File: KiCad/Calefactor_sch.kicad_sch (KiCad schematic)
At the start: 3 parts, among them U1 SHTC3

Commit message: calefactor-Usart
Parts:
- added Q13: AO3400A, Package_TO_SOT_SMD:SOT-23, symbol Transistor_FET:AO3400A
- added R7: Heater, symbol Device:Heater
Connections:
- net GND: now also R7.2
- new net: Q13.2 (S), R7.1
- new net 5V: Q13.3 (D)

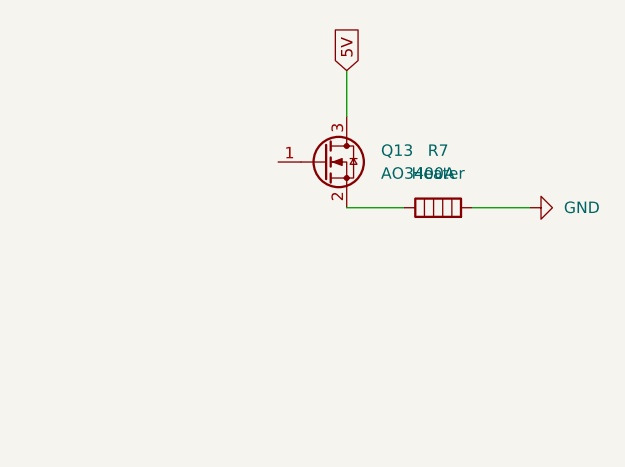
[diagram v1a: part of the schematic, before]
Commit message: añadido conexiones del PIC y cambiado lógica de los drivers para reducir pines
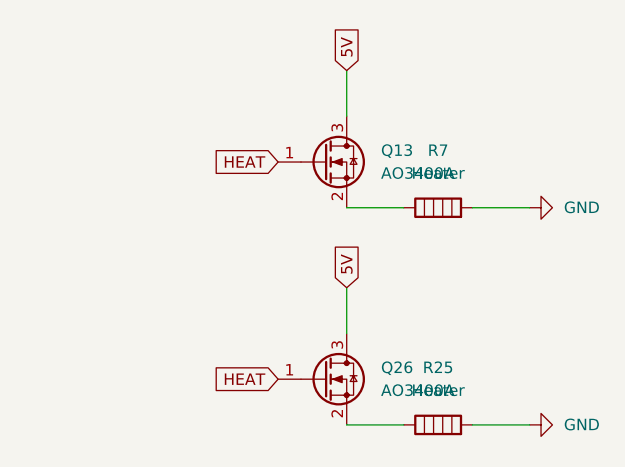
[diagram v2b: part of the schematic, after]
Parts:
- added Q26: AO3400A, Package_TO_SOT_SMD:SOT-23, symbol Transistor_FET:AO3400A
- added R25: Heater, symbol Device:Heater
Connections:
- net 5V: now also Q26.3 (D)
- net GND: now also R25.2
- net HEAT: now reaches Q13.1 (G)
- net HEAT: now also Q26.1 (G)
- new net: Q26.2 (S), R25.1

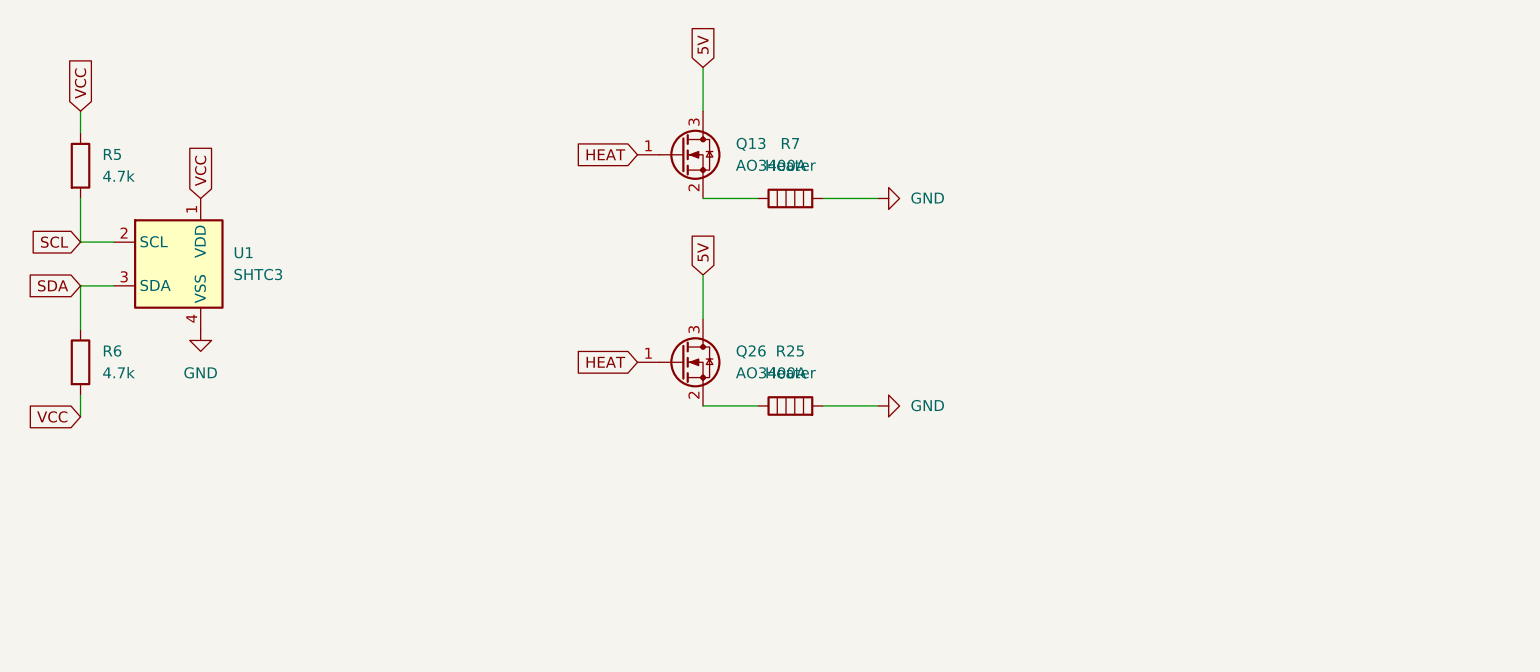
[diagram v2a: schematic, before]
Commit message: canvis organització y reles calefactor
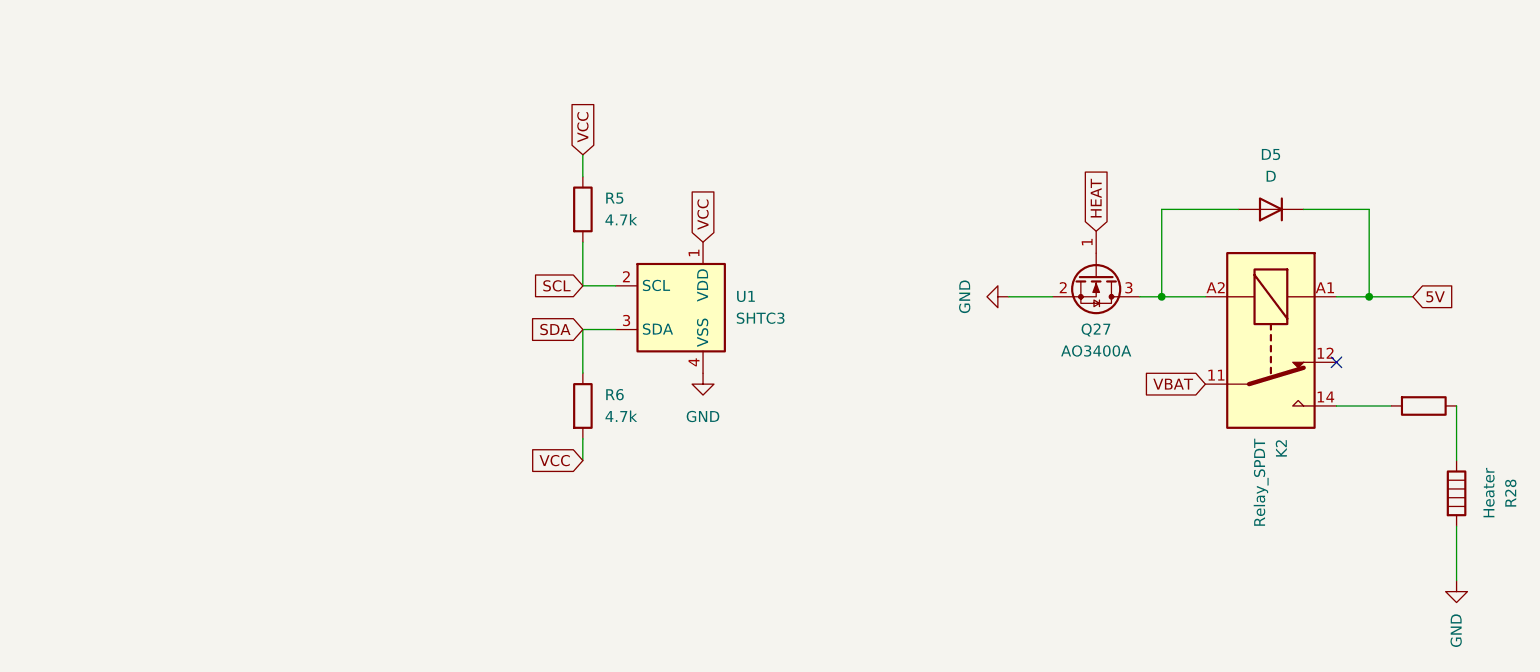
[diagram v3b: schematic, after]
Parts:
- removed Q13, Q26: AO3400A, Package_TO_SOT_SMD:SOT-23, symbol Transistor_FET:AO3400A
- removed R25, R7: Heater, symbol Device:Heater
- added D5: D, symbol Device:D
- added K2: Relay_SPDT, symbol Relay:Relay_SPDT
- added Q27: AO3400A, Package_TO_SOT_SMD:SOT-23, symbol Transistor_FET:AO3400A
- added R28: Heater, symbol Device:Heater
- added R29: R, symbol Device:R
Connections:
- net 5V: now also D5.1 (K), K2.A1
- net GND: now also Q27.2 (S), R28.2
- net HEAT: now also Q27.1 (G)
- new net: R28.1, R29.1
- new net: K2.14, R29.2
- new net: D5.2 (A), K2.A2, Q27.3 (D)
- new net VBAT: K2.11
- no-connect marks 0 -> 1
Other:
- moved on the sheet: R5, R6, U1

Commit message: reducido motores y finales de carrera
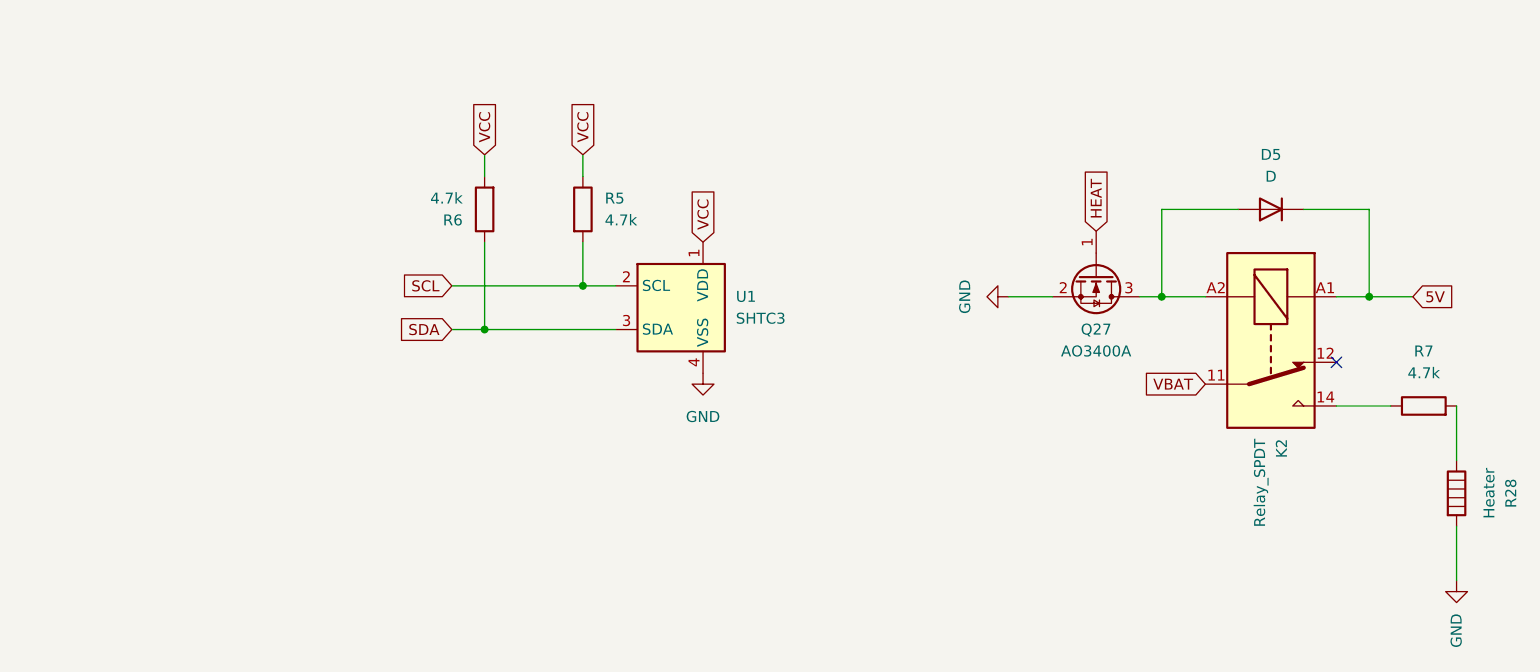
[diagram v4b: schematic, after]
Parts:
- removed R29: R, symbol Device:R
- added R7: 4.7k, symbol Device:R
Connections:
- net at R28.1: now also R7.2
- net at K2.14: now also R7.1
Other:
- moved on the sheet: R6

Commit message: he añadido huelas a algunos componentes importates
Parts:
- K2: footprint (none) -> Button_Switch_SMD:SW_Push_1P1T_NO_E-Switch_TL3301NxxxxxG
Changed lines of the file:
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@@
 			)
 		)
-		(property "Footprint" ""
+		(property "Footprint" "Button_Switch_SMD:SW_Push_1P1T_NO_E-Switch_TL3301NxxxxxG"
 			(at 172.72 87.63 0)
 			(effects

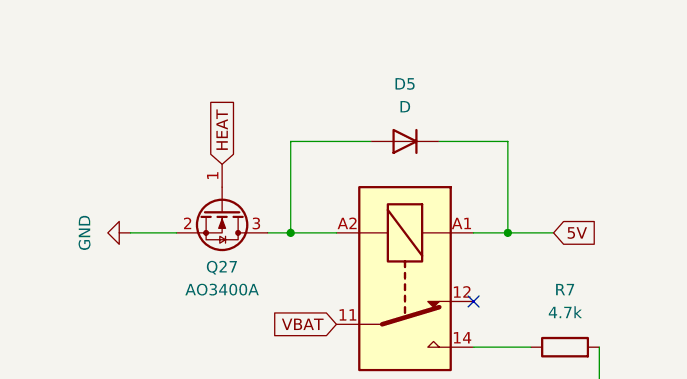
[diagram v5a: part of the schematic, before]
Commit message: he añadido el resto de huellas, he corregido algunos errores en la parte de alimentación en los diodos. tambien he trasladados todas las huellas a la pcb y lo he intentado separar un poco para verlo mas claro cuando empecemos el placing.
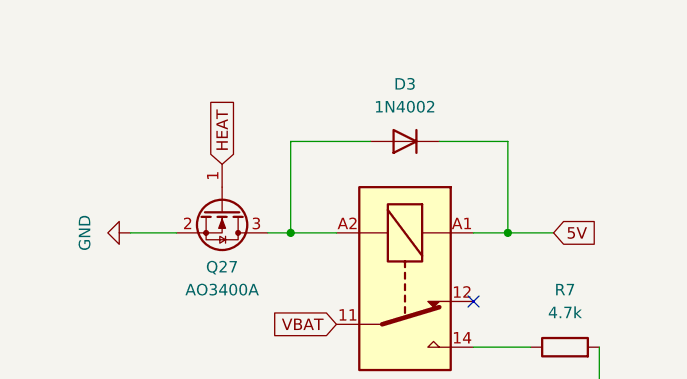
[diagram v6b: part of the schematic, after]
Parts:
- removed D5: D, symbol Device:D
- added D3: 1N4002, Diode_THT:D_DO-41_SOD81_P2.54mm_Vertical_AnodeUp, symbol Diode:1N4002
- R5, R6: footprint (none) -> Resistor_SMD:R_0402_1005Metric
- R7: footprint (none) -> Resistor_SMD:R_0603_1608Metric
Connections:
- net 5V: now also D3.1 (K)
- net at K2.A2, Q27.3 (D): now also D3.2 (A)
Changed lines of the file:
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@@
 			)
 		)
-		(property "Footprint" ""
+		(property "Footprint" "Resistor_SMD:R_0603_1608Metric"
 			(at 191.77 85.598 90)
 			(effects
@@
 	)
 	(symbol
+		(lib_id "Diode:1N4002")
+		(at 173.99 60.96 180)
+		(unit 1)
+		(exclude_from_sim no)
+		(in_bom yes)
+		(on_board yes)
+		(dnp no)
+		(fields_autoplaced yes)
+		(property "Reference" "D3"
+			(at 173.99 54.61 0)
+			(effects
+				(font
+					(size 1.27 1.27)
+				)
+			)
+		)
+		(property "Value" "1N4002"
+			(at 173.99 57.15 0)
+			(effects
+				(font
+					(size 1.27 1.27)
+				)
+			)
+		)
+		(property "Footprint" "Diode_THT:D_DO-41_SOD81_P2.54mm_Vertical_AnodeUp"
+			(at 173.99 56.515 0)
+			(effects
+				(font
+					(size 1.27 1.27)
+				)
+				(hide yes)
+			)
+		)
+		(property "Datasheet" "http://www.vishay.com/docs/88503/1n4001.pdf"
+			(at 173.99 60.96 0)
+			(effects
+				(font
+					(size 1.27 1.27)
+				)
+				(hide yes)
+			)
+		)
+		(property "Description" "100V 1A General Purpose Rectifier Diode, DO-41"
+			(at 173.99 60.96 0)
+			(effects
+				(font
+					(size 1.27 1.27)
+				)
+				(hide yes)
+			)
+		)
+		(property "Sim.Device" "D"
+			(at 173.99 60.96 0)
+			(effects
+				(font
+					(size 1.27 1.27)
+				)
+				(hide yes)
+			)
+		)
+		(property "Sim.Pins" "1=K 2=A"
+			(at 173.99 60.96 0)
+			(effects
+				(font
+					(size 1.27 1.27)
+				)
+				(hide yes)
+			)
+		)
+		(pin "1"
+		)
+		(pin "2"
+		)
+		(instances
+			(project ""
+				(path "/9b9f005f-0621-4675-bd4e-683e7082b120/1a76def2-ddde-4ac6-93d0-da3d16171b62"
+					(reference "D3")
+					(unit 1)
+				)
+			)
+		)
+	)
+	(symbol
 		(lib_id "Relay:Relay_SPDT")
 		(at 173.99 76.2 270)
@@
 			)
 		)
-		(property "Footprint" ""
+		(property "Footprint" "Resistor_SMD:R_0402_1005Metric"
 			(at 84.328 60.96 90)
 			(effects
@@
 			)
 		)
-		(property "Footprint" ""
+		(property "Footprint" "Resistor_SMD:R_0402_1005Metric"
 			(at 92.202 60.96 90)
 			(effects
@@
 					(unit 1)
 				)
-			)
-		)
-	)
-	(symbol
-		(lib_id "Device:D")
-		(at 173.99 60.96 180)
-		(unit 1)
-		(exclude_from_sim no)
-		(in_bom yes)
-		(on_board yes)
-		(dnp no)
-		(fields_autoplaced yes)
-		(property "Reference" "D5"
-			(at 173.99 54.61 0)
-			(effects
-				(font
-					(size 1.27 1.27)
-				)
-			)
-		)
-		(property "Value" "D"
-			(at 173.99 57.15 0)
-			(effects
-				(font
-					(size 1.27 1.27)
-				)
-			)
-		)
-		(property "Footprint" ""
-			(at 173.99 60.96 0)
-			(effects
-				(font
-					(size 1.27 1.27)
-				)
-				(hide yes)
-			)
-		)
-		(property "Datasheet" "~"
-			(at 173.99 60.96 0)
-			(effects
-				(font
-					(size 1.27 1.27)
-				)
-				(hide yes)
-			)
-		)
-		(property "Description" "Diode"
-			(at 173.99 60.96 0)
-			(effects
-				(font
-					(size 1.27 1.27)
-				)
-				(hide yes)
-			)
-		)
-		(property "Sim.Device" "D"
-			(at 173.99 60.96 0)
-			(effects
-				(font
-					(size 1.27 1.27)
-				)
-				(hide yes)
-			)
-		)
-		(property "Sim.Pins" "1=K 2=A"
-			(at 173.99 60.96 0)
-			(effects
-				(font
-					(size 1.27 1.27)
-				)
-				(hide yes)
-			)
-		)
-		(pin "1"
-		)
-		(pin "2"
-		)
-		(instances
-			(project ""
-				(path "/9b9f005f-0621-4675-bd4e-683e7082b120/1a76def2-ddde-4ac6-93d0-da3d16171b62"
-					(reference "D5")
-					(unit 1)
-				)

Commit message: Resto de huellas
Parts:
- R28: footprint (none) -> Resistor_THT:R_Axial_Power_L20.0mm_W6.4mm_P5.08mm_Vertical
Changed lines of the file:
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@@
 			)
 		)
-		(property "Footprint" ""
+		(property "Footprint" "Resistor_THT:R_Axial_Power_L20.0mm_W6.4mm_P5.08mm_Vertical"
 			(at 193.802 93.98 90)
 			(effects

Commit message: cambiado layout general
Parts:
- K2: footprint Button_Switch_SMD:SW_Push_1P1T_NO_E-Switch_TL3301NxxxxxG -> Relay_THT:Relay_1-Form-C_Schrack-RYII_RM3.2mm
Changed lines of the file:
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@@
 			)
 		)
-		(property "Footprint" "Button_Switch_SMD:SW_Push_1P1T_NO_E-Switch_TL3301NxxxxxG"
+		(property "Footprint" "Relay_THT:Relay_1-Form-C_Schrack-RYII_RM3.2mm"
 			(at 172.72 87.63 0)
 			(effects
